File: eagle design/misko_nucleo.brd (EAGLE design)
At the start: 115 x 73 mm, 99 parts, among them CN1 LiPo Battery, IC101 ADXL345, IC102 74HCT1G32GW, IC2 TPS63031, IC3 FT230XS, IC4 RN4678_BT_MODULE, IC5 DS1394U-33+, IC6 MAX6818, IC7 SP3012-04UTG, Q2 BSS84, Q3 LFXTAL016178R, SW1 MICROJOYSTICK, SW2 PB6156RSL, SW3 PB6156RSL, U1 SN74LVC1G3157DBVR - BT switch, U2 ATMEGA1281-16AU, U4 MCP73871-2AAI/ML, U5 SN74LVC1G3157DBVR - GPS switch, X1 FH12-30S-0.5SH

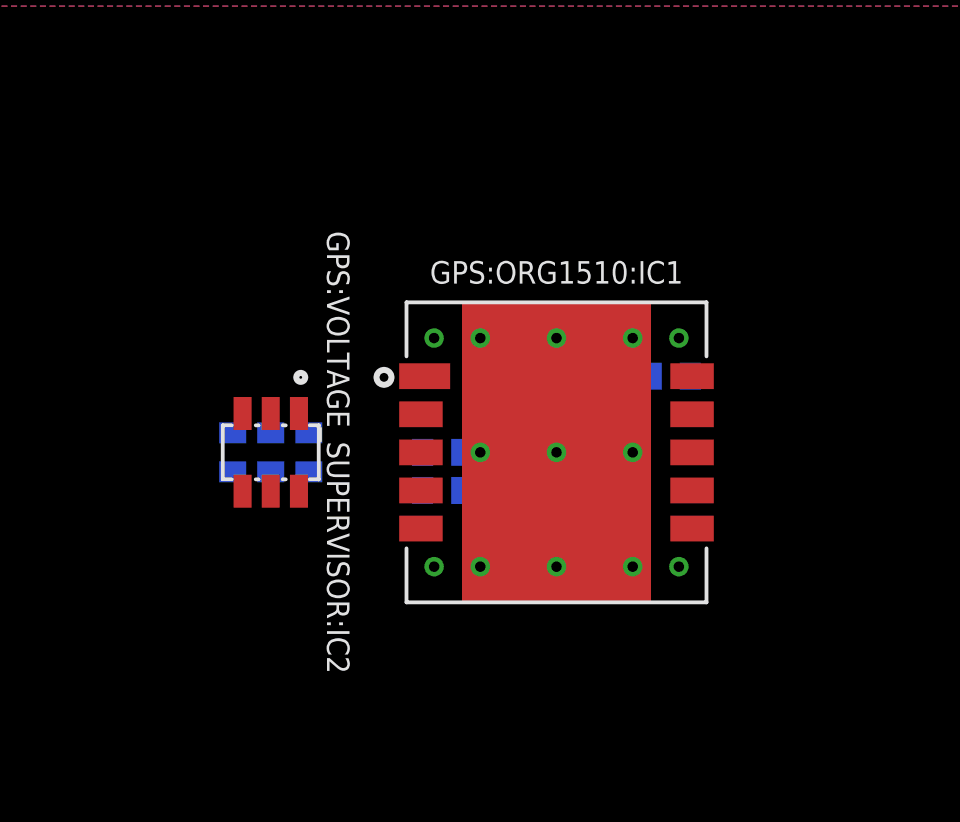
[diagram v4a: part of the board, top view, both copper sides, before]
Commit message: - updated ORG1510 library - added low pass filter to GPS module UART pins
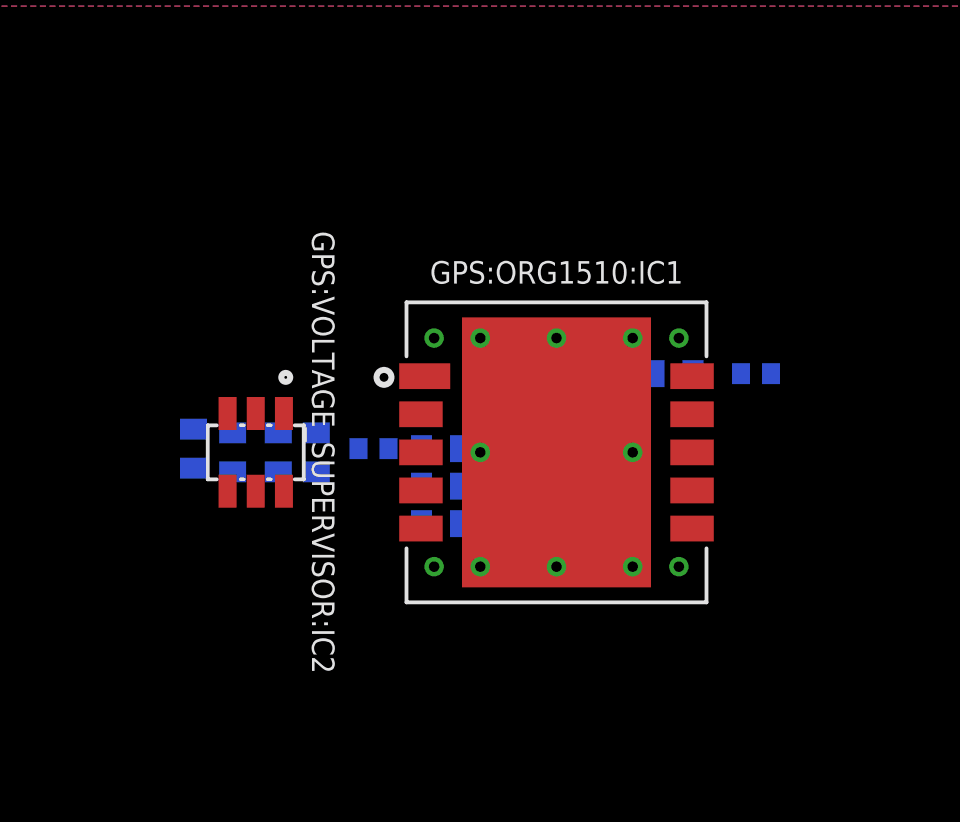
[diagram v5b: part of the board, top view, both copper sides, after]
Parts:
- added GPS:ORG1510:C1: 0.1u / 16V, resistor:C0402
- added GPS:ORG1510:R1, GPS:ORG1510:R2: 33R, rcl:R0402
- added GPS:VOLTAGE_SUPERVISOR:R1: 100k, resistor:R0402
- GPS:ORG1510:C22, GPS:ORG1510:C31: value 18p / 16V -> 33p / 16V
- GPS:VOLTAGE_SUPERVISOR:C1: value 1n / 16V -> 0.1u / 16V
- GPS:VOLTAGE_SUPERVISOR:R18: value 1M -> 100k
- moved GPS:VOLTAGE_SUPERVISOR:IC2 0.50 mm to (28.1, -15.9)
- moved GPS:VOLTAGE_SUPERVISOR:C2 0.25 mm to (28.8, -15.9)
- moved GPS:VOLTAGE_SUPERVISOR:R18 0.25 mm to (30.1, -15.9)
- moved GPS:ORG1510:C2 0.15 mm to (34.2, -17.0)
- moved GPS:ORG1510:C22 0.13 mm to (34.2, -15.8)
- moved GPS:ORG1510:C31 0.12 mm to (42.0, -13.2)
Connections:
- new net GPS:ORG1510:GPS_RX: GPS:ORG1510:C31.1, GPS:ORG1510:IC1.RX_10, GPS:ORG1510:R2.2
- new net GPS:ORG1510:GPS_TX: GPS:ORG1510:C22.1, GPS:ORG1510:IC1.3_TX, GPS:ORG1510:R1.2
- new net GPS:VOLTAGE_SUPERVISOR:CT: GPS:VOLTAGE_SUPERVISOR:IC2.CT, GPS:VOLTAGE_SUPERVISOR:R1.1
- net 3V3: now also GPS:VOLTAGE_SUPERVISOR:R1.2
- net GND: now also GPS:ORG1510:C1.2; no longer GPS:ORG1510:IC1.GND11
- net GPS:VGPS: now also GPS:ORG1510:C1.1
- net GPS_SW_SERIAL_TX: now also GPS:ORG1510:R2.1; no longer GPS:ORG1510:C31.1, GPS:ORG1510:IC1.RX_10
- net GPS_TX: now also GPS:ORG1510:R1.1; no longer GPS:ORG1510:C22.1, GPS:ORG1510:IC1.3_TX

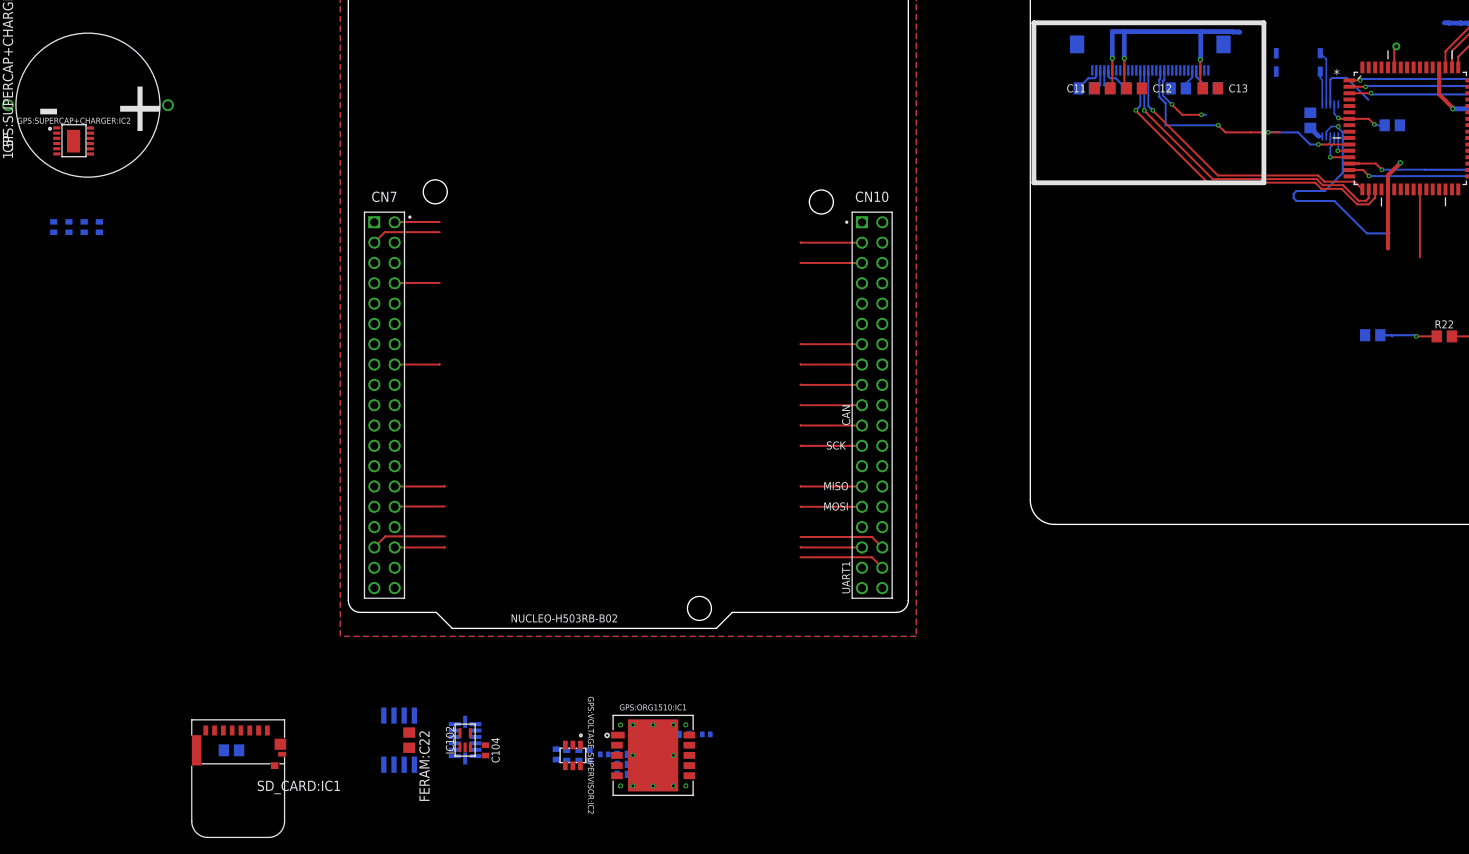
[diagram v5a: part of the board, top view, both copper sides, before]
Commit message: - removed RTC IC
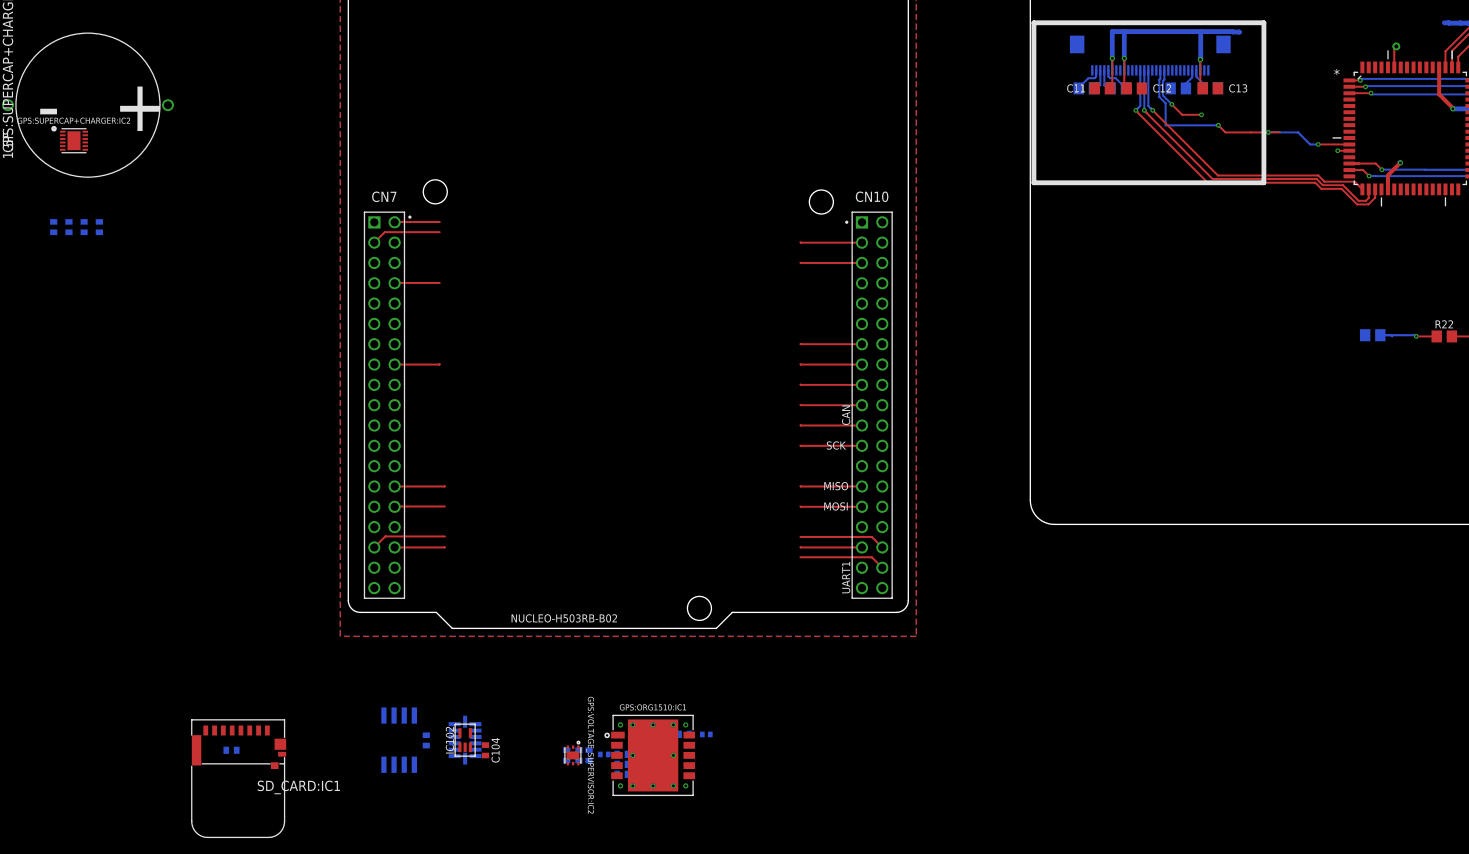
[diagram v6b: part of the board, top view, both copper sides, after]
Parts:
- removed C21: 0.1µF, rcl:C0805
- removed FERAM:C22: 0.1u / 16V, rcl:C0805
- removed GPS:VOLTAGE_SUPERVISOR:R1: 100k, resistor:R0402
- removed IC5: DS1394U-33+, DS1394U-33+ RTC SPI Module:10UMAX
- removed Q3: LFXTAL016178R, LFXTAL016178R 32.768kHz crystal:SMD
- removed R26: 10k, rcl:R0805
- added FERAM:C1: 0.1u / 16V, rcl:C0402
- GPS:SUPERCAP+CHARGER:IC2: value (none) -> LTC4425EDD#PBF; device LTC4425 Supercap Charger:MSOP-12 -> LTC4425 Supercap Charger:DFN-12
- GPS:VOLTAGE_SUPERVISOR:IC2: device TPS3808 - Supervisory Circuit:SOT23-6 -> TPS3808 - Supervisory Circuit:WSON-6
- SD_CARD:C31: device rcl:C0805 -> rcl:C0402
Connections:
- net GPS_SW_SERIAL_TX renamed GPS_MCU_RX
- net GPS_TX renamed GPS_MCU_TX
- removed net RTC_XTAL1: IC5.X1, Q3.XTAL1
- removed net RTC_XTAL2: IC5.X2, Q3.XTAL2
- removed net VGPS: IC5.VBACK
- net 3V3: now also FERAM:C1.1; no longer FERAM:C22.1, GPS:VOLTAGE_SUPERVISOR:R1.2
- net GND: now also FERAM:C1.2, GPS:VOLTAGE_SUPERVISOR:IC2.GND1, GPS:VOLTAGE_SUPERVISOR:IC2.GND2; no longer C21.2, FERAM:C22.2, GPS:VOLTAGE_SUPERVISOR:IC2.GND, IC5.GND
- net GPS:VOLTAGE_SUPERVISOR:CT: no longer GPS:VOLTAGE_SUPERVISOR:R1.1
- net RTC_INT_INTERRUPT_PIN: no longer IC5.!INT!
- net SPI_MISO_PIN: no longer IC5.DOUT
- net SPI_MOSI_PIN: no longer IC5.DIN
- net SPI_SCK_PIN: no longer IC5.SCLK
- net SPI_SS_RTC_PIN: no longer IC5.!CS!, R26.2
- net VCC: no longer C21.1, IC5.VCC, R26.1
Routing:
- net RTC_INT_INTERRUPT_PIN: track 38.7 -> 0.00 mm, vias 1 -> 0
- net VCC: track 275.0 -> 265.7 mm
- net VGPS: track 9.08 -> 0.00 mm
- net SPI_SS_RTC_PIN: track 8.09 -> 0.00 mm, vias 2 -> 0
- net RTC_XTAL2: track 6.71 -> 0.00 mm
- net SPI_MISO_PIN: track 5.19 -> 0.00 mm, vias 1 -> 0
- net RTC_XTAL1: track 4.20 -> 0.00 mm
- net SPI_MOSI_PIN: track 12.9 -> 10.5 mm
- net SPI_SCK_PIN: track 35.3 -> 33.0 mm
